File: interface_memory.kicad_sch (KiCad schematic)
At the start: 45 parts, among them IC304 ?, IC509 M41464, IC510 M41464, IC512 LC3517BML, IC516 74LS244, IC517 74LS244, IC518 74LS244, IC519 74F32, IC520 74LS245

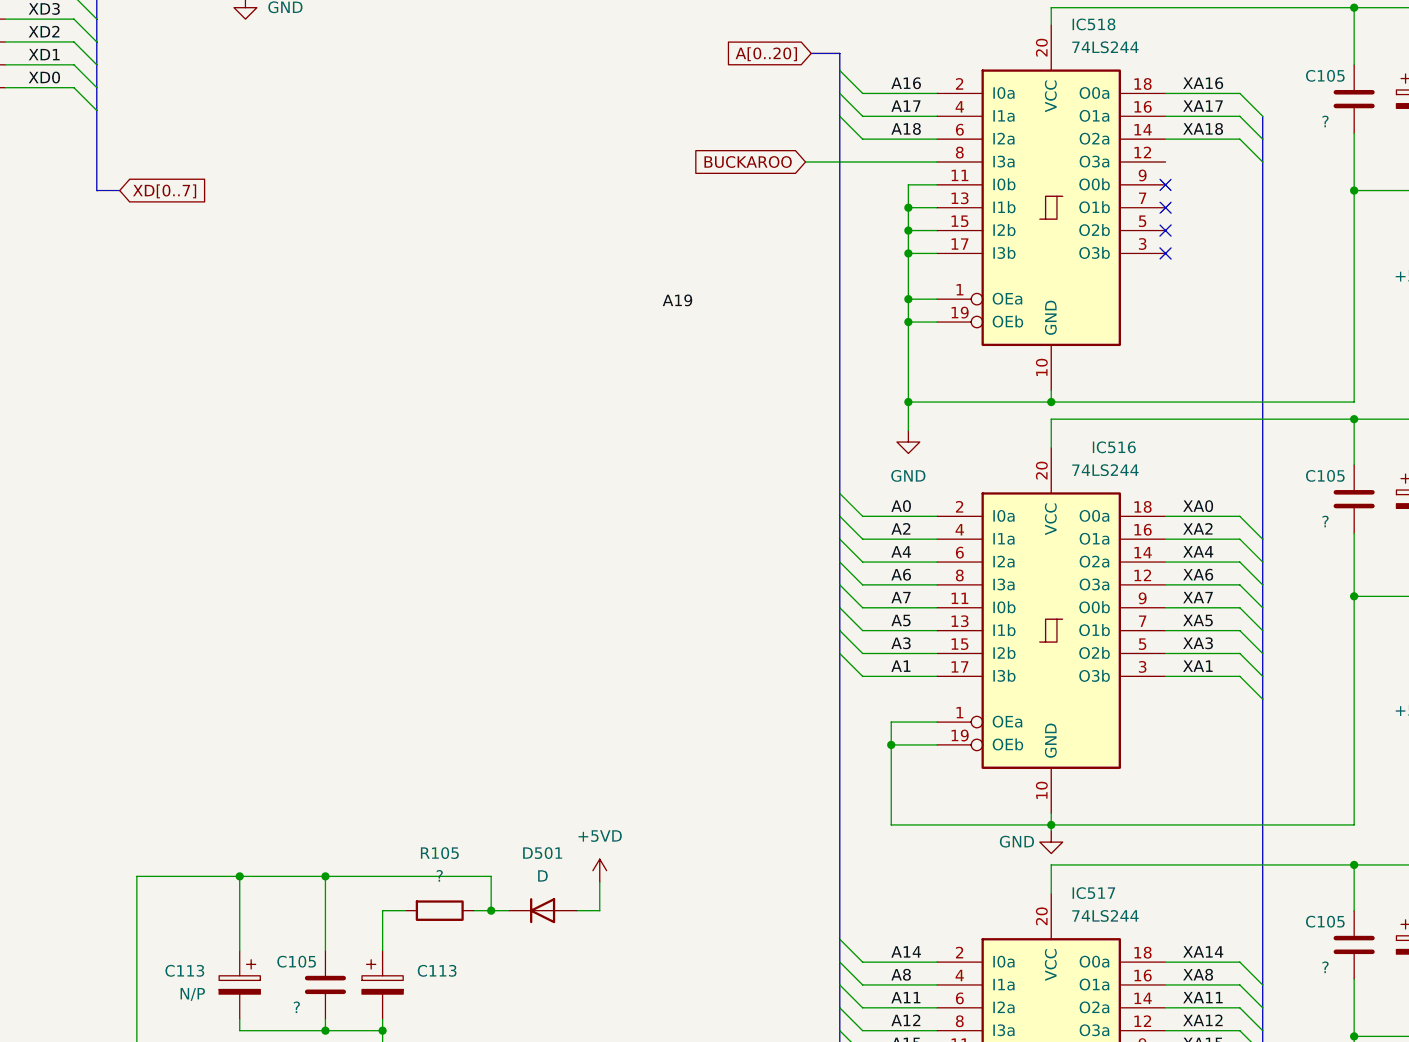
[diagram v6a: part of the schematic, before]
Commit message: Yet more passives on back.
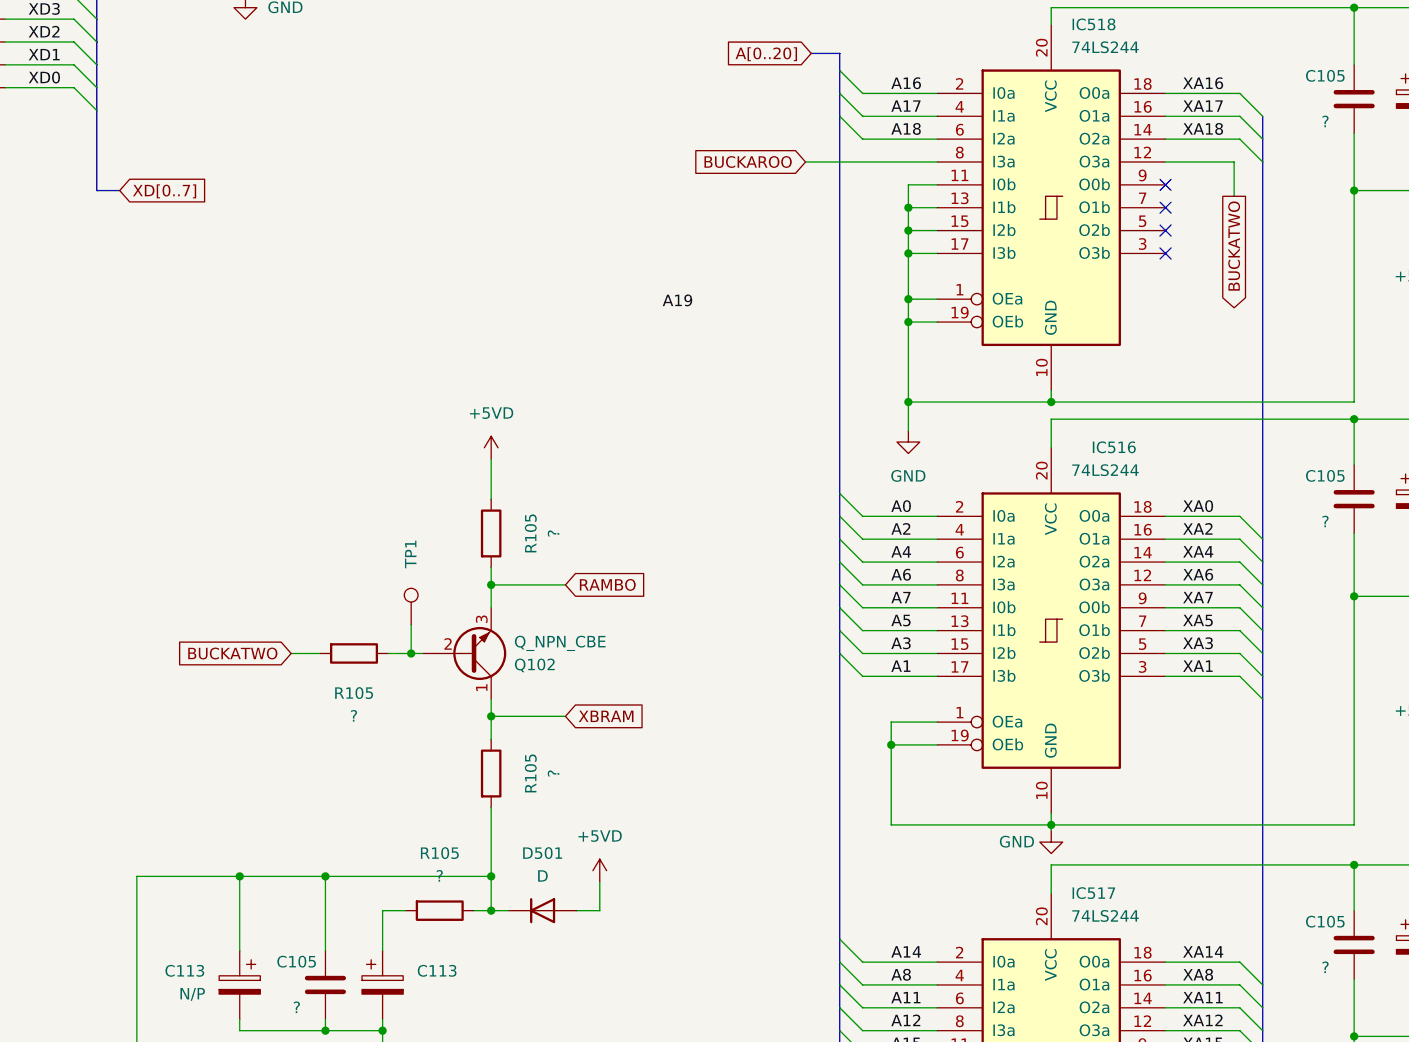
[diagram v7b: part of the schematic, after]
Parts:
- added Q102: Q_NPN_CBE, A-PCENGINE:Transistor_SMD, symbol Device:Q_NPN_CBE
- added R105 (x3): ?, A-PCENGINE:SMD_0805_Narrow_Long, symbol Device:R
- added TP1: ~, A-PCENGINE:Test_Point_1.5mm, symbol Connector:TestPoint
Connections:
- net +5VD: now also R105.1
- net at C105.2, C113.1, D501.1 (K)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: now also R105.2
- net BUCKATWO: now reaches IC518.12 (O3a)
- net BUCKATWO: now also R105.2
- new net: Q102.2 (B), R105.1, TP1.1
- new net RAMBO: Q102.3 (E), R105.2
- new net XBRAM: Q102.1 (C), R105.1

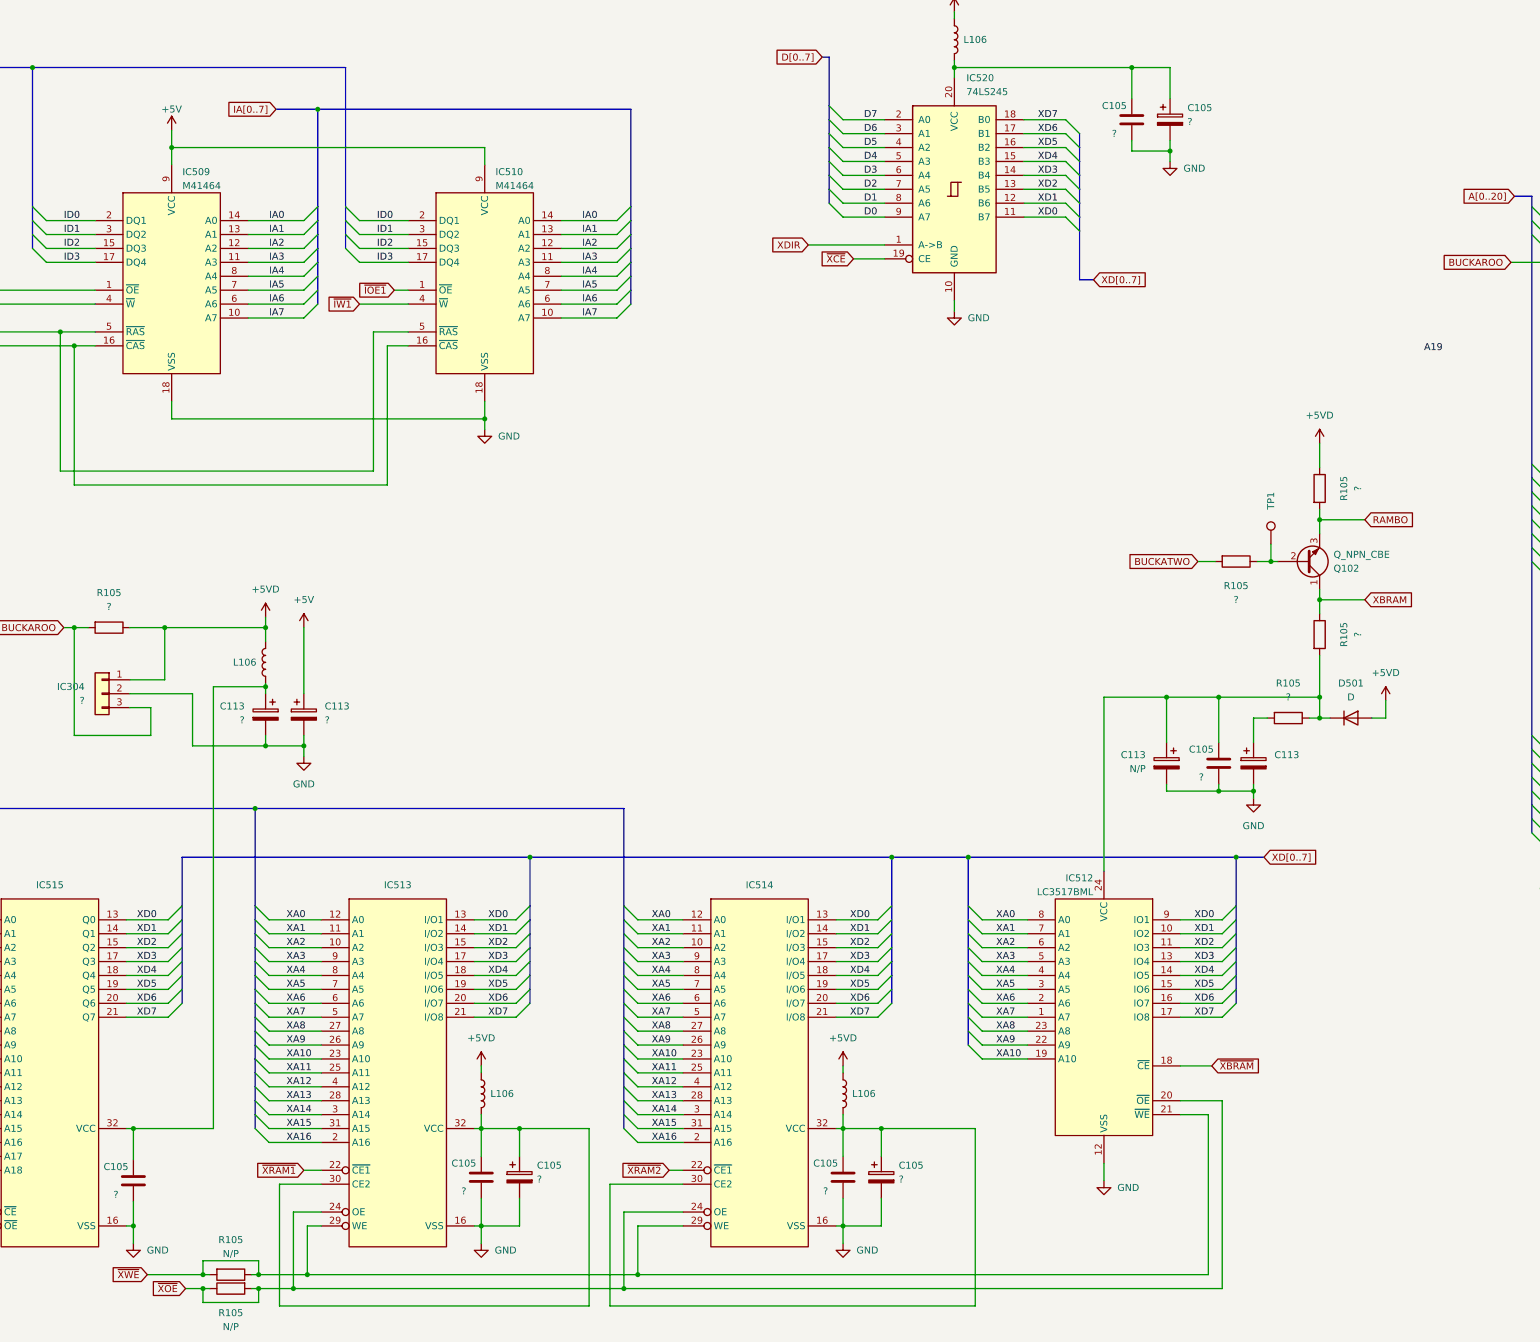
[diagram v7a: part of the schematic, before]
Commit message: Fix DRC errors.
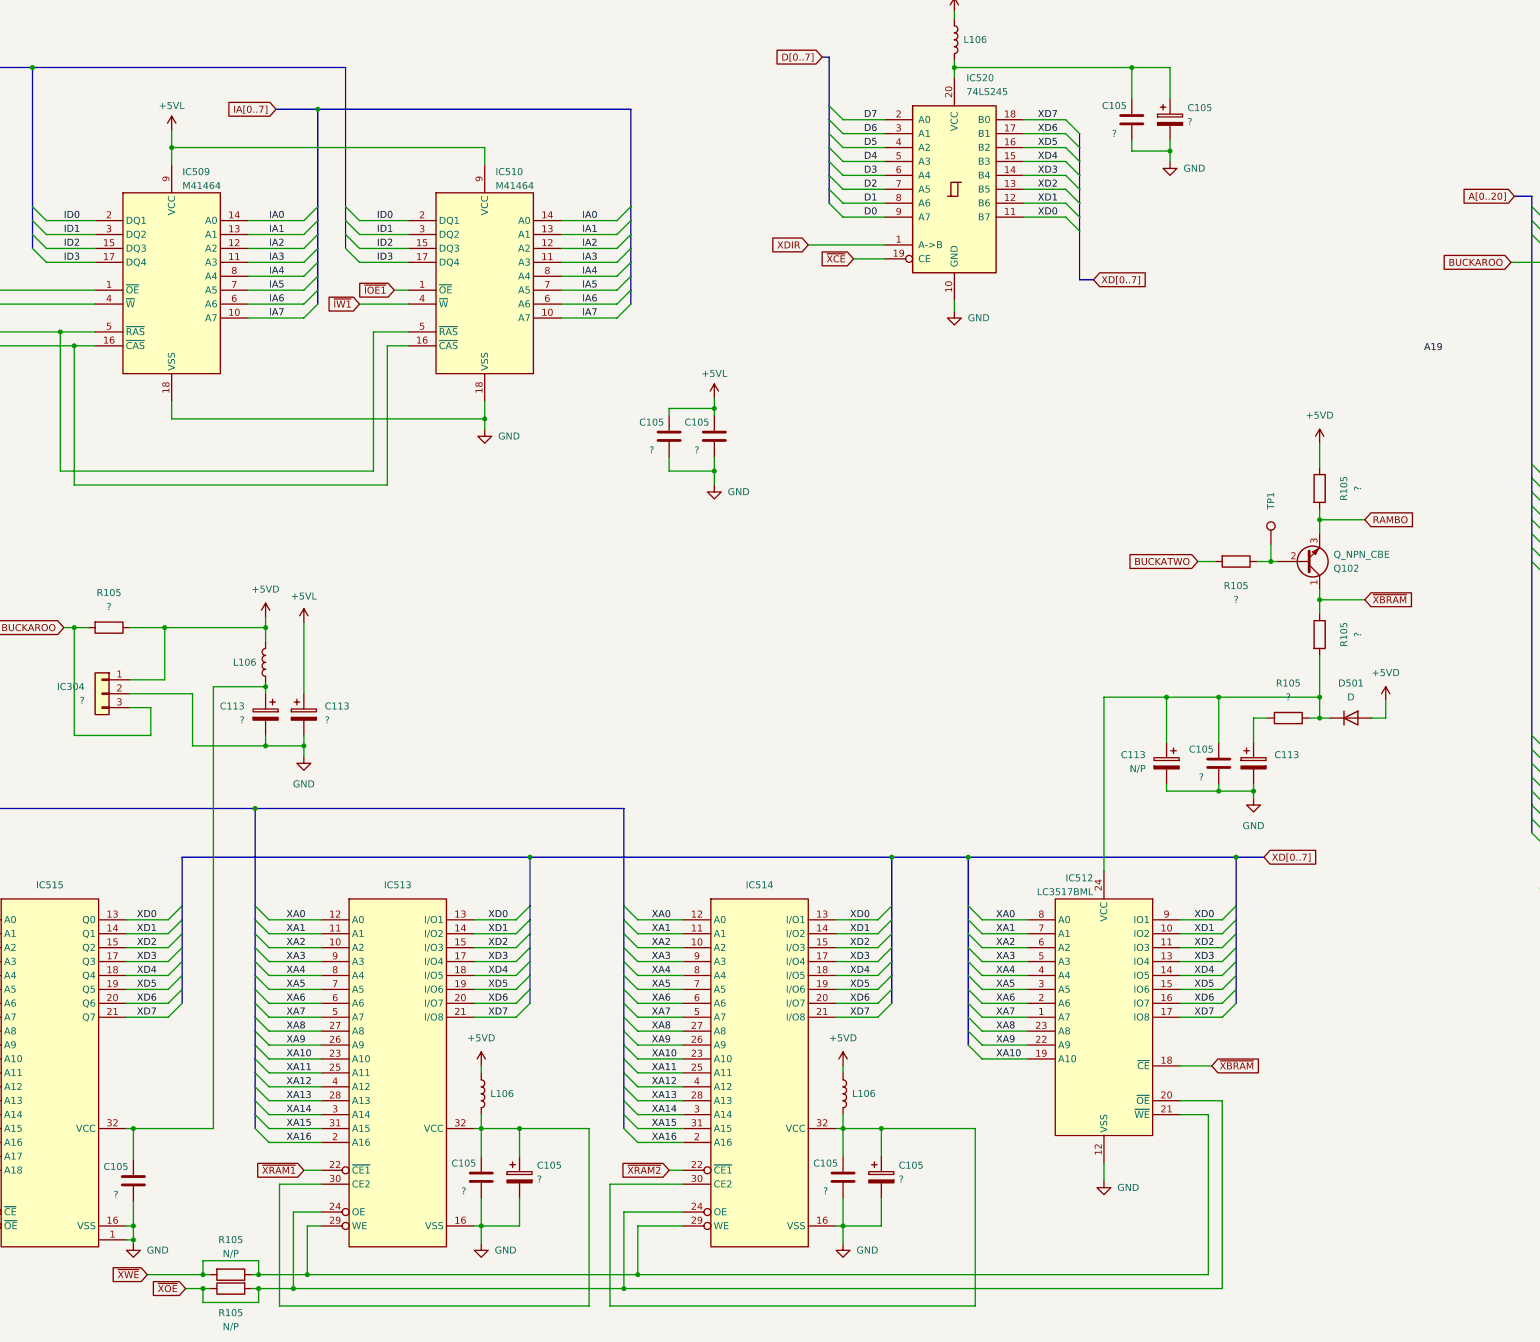
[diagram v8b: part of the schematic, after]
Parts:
- added C105 (x2): ?, A-PCENGINE:SMD_0805_Narrow_Long, symbol Device:C
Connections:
- net XBRAM is gone; now on net ~{XBRAM}: Q102.1 (C), R105.1
- net GND: now also IC515.1, C105.1, C105.1
- net +5V renamed +5VL
- net +5VL: now also C105.2, C105.2
